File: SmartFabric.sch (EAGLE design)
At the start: 1 part

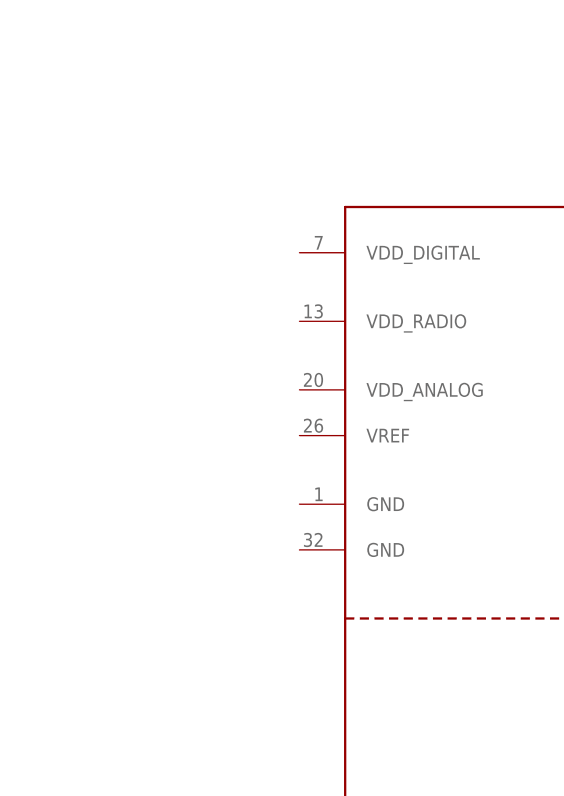
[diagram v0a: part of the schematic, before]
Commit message: added gitignore and wired power and added a ferrite bead
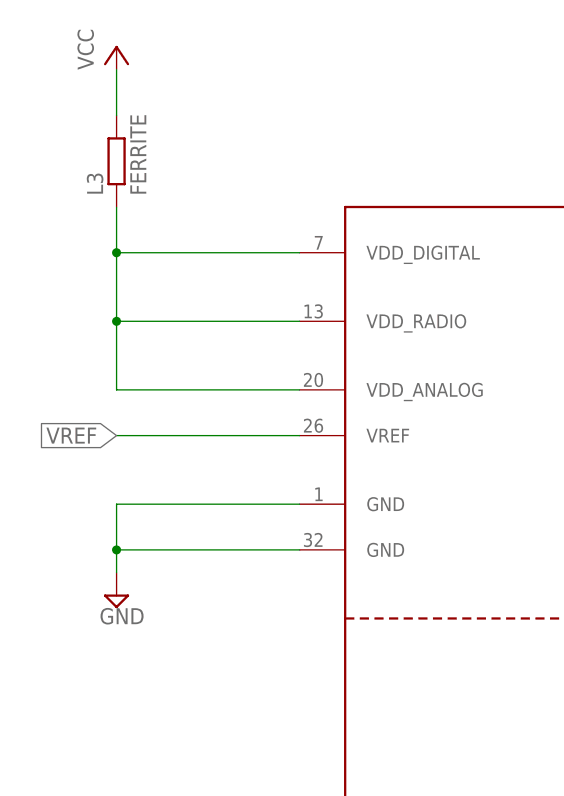
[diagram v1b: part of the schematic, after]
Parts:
- added L3: FERRITE, rcl:R-EU_R0805
- renumbered U$1 to U1
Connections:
- new net GND: U1.GND@1, U1.GND@2
- new net N$1: L3.1, U1.VDD_ANALOG, U1.VDD_DIGITAL, U1.VDD_RADIO
- new net VCC: L3.2
- new net VREF: U1.VREF
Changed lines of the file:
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@@
 <layer number="113" name="IDFDebug" color="4" fill="1" visible="yes" active="yes"/>
 <layer number="116" name="Patch_BOT" color="9" fill="4" visible="yes" active="yes"/>
+<layer number="118" name="Rect_Pads" color="7" fill="1" visible="no" active="yes"/>
 <layer number="121" name="_tsilk" color="7" fill="1" visible="yes" active="yes"/>
 <layer number="122" name="_bsilk" color="7" fill="1" visible="yes" active="yes"/>
@@
 <layer number="223" name="223bmp" color="24" fill="1" visible="no" active="no"/>
 <layer number="224" name="224bmp" color="25" fill="1" visible="no" active="no"/>
+<layer number="231" name="Eagle3D_PG1" color="7" fill="1" visible="yes" active="yes"/>
+<layer number="232" name="Eagle3D_PG2" color="7" fill="1" visible="yes" active="yes"/>
+<layer number="233" name="Eagle3D_PG3" color="7" fill="1" visible="yes" active="yes"/>
 <layer number="248" name="Housing" color="7" fill="1" visible="yes" active="yes"/>
 <layer number="249" name="Edge" color="7" fill="1" visible="yes" active="yes"/>
@@
 <parts>
 <part name="FRAME1" library="frames" deviceset="FRAME_B_L" device=""/>
-<part name="U$1" library="wicked-device" deviceset="CYPRESS-EZ-BLE-PSOC" device=""/>
+<part name="U1" library="wicked-device" deviceset="CYPRESS-EZ-BLE-PSOC" device=""/>
+<part name="P+1" library="supply1" deviceset="VCC" device=""/>
+<part name="SUPPLY1" library="supply2" deviceset="GND" device=""/>
+<part name="L3" library="rcl" deviceset="R-EU_" device="R0805" value="FERRITE"/>
 </parts>
 <sheets>
@@
 <instance part="FRAME1" gate="G$1" x="0" y="0"/>
 <instance part="FRAME1" gate="G$2" x="325.12" y="0"/>
-<instance part="U$1" gate="G$1" x="213.36" y="38.1"/>
+<instance part="U1" gate="G$1" x="213.36" y="38.1"/>
+<instance part="P+1" gate="VCC" x="149.86" y="251.46"/>
+<instance part="SUPPLY1" gate="GND" x="149.86" y="190.5"/>
+<instance part="L3" gate="G$1" x="149.86" y="238.76" rot="R90"/>
 </instances>
 <busses>
 </busses>
 <nets>
+<net name="GND" class="0">
+<segment>
+<pinref part="U1" gate="G$1" pin="GND@1"/>
+<pinref part="SUPPLY1" gate="GND" pin="GND"/>
+<wire x1="170.18" y1="200.66" x2="149.86" y2="200.66" width="0.1524" layer="91"/>
+<wire x1="149.86" y1="200.66" x2="149.86" y2="195.58" width="0.1524" layer="91"/>
+<pinref part="U1" gate="G$1" pin="GND@2"/>
+<wire x1="149.86" y1="195.58" x2="149.86" y2="193.04" width="0.1524" layer="91"/>
+<wire x1="170.18" y1="195.58" x2="149.86" y2="195.58" width="0.1524" layer="91"/>
+<junction x="149.86" y="195.58"/>
+</segment>
+</net>
+<net name="N$1" class="0">
+<segment>
+<pinref part="U1" gate="G$1" pin="VDD_ANALOG"/>
+<pinref part="L3" gate="G$1" pin="1"/>
+<wire x1="170.18" y1="213.36" x2="149.86" y2="213.36" width="0.1524" layer="91"/>
+<wire x1="149.86" y1="213.36" x2="149.86" y2="220.98" width="0.1524" layer="91"/>
+<pinref part="U1" gate="G$1" pin="VDD_RADIO"/>
+<wire x1="149.86" y1="220.98" x2="149.86" y2="228.6" width="0.1524" layer="91"/>
+<wire x1="149.86" y1="228.6" x2="149.86" y2="233.68" width="0.1524" layer="91"/>
+<wire x1="170.18" y1="220.98" x2="149.86" y2="220.98" width="0.1524" layer="91"/>
+<junction x="149.86" y="220.98"/>
+<pinref part="U1" gate="G$1" pin="VDD_DIGITAL"/>
+<wire x1="170.18" y1="228.6" x2="149.86" y2="228.6" width="0.1524" layer="91"/>
+<junction x="149.86" y="228.6"/>
+</segment>
+</net>
+<net name="VCC" class="0">
+<segment>
+<pinref part="L3" gate="G$1" pin="2"/>
+<pinref part="P+1" gate="VCC" pin="VCC"/>
+<wire x1="149.86" y1="243.84" x2="149.86" y2="248.92" width="0.1524" layer="91"/>
+</segment>
+</net>
+<net name="VREF" class="0">
+<segment>
+<pinref part="U1" gate="G$1" pin="VREF"/>
+<wire x1="170.18" y1="208.28" x2="149.86" y2="208.28" width="0.1524" layer="91"/>
+<label x="149.86" y="208.28" size="1.778" layer="95" rot="R180" xref="yes"/>
+</segment>
+</net>
 </nets>
 </sheet>
